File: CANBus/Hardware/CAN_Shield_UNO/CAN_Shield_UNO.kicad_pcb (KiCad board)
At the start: 2 copper layers, 68.6 x 53.3 mm, 15 parts, among them J1 Power, J2 Digital/PWM, J3 Analog, J4 Digital/PWM, J7 Screw_Terminal_01x02, U2 TCAN1051HGV

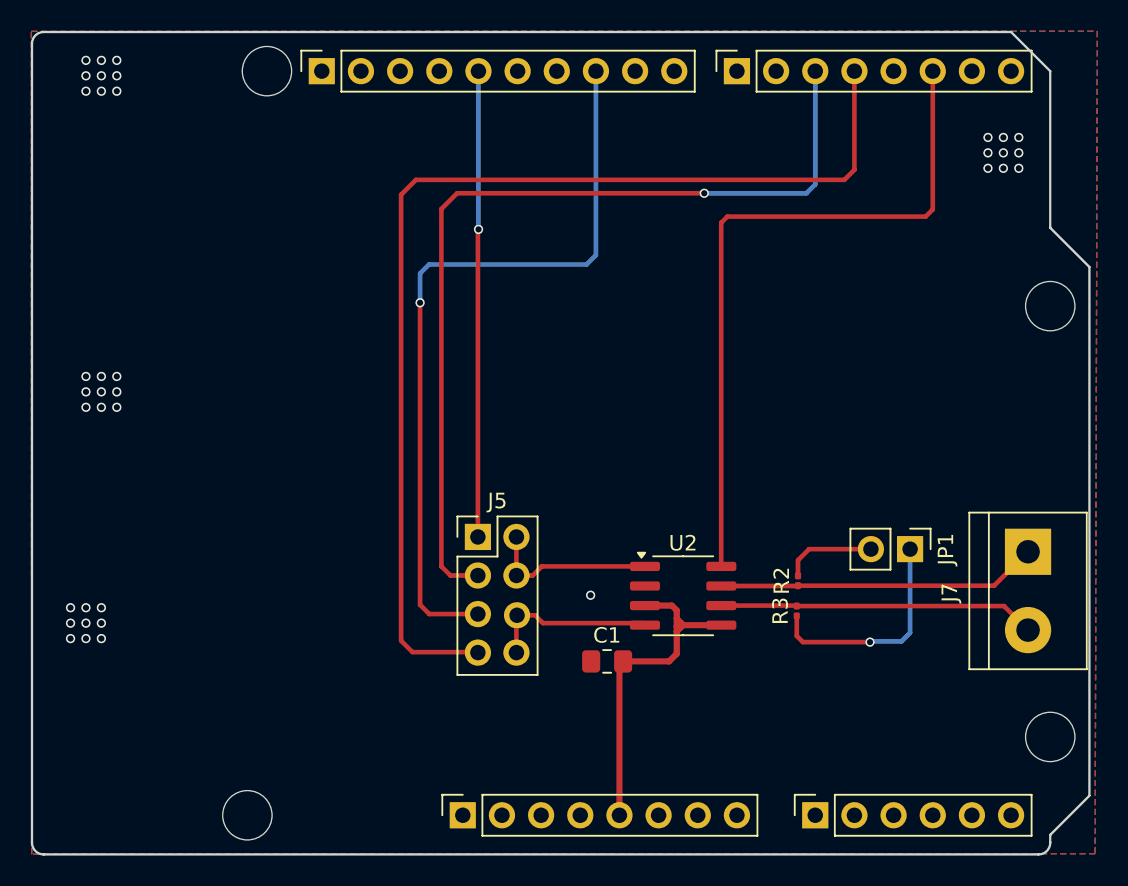
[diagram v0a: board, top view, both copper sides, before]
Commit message: feat: Resistors got changed
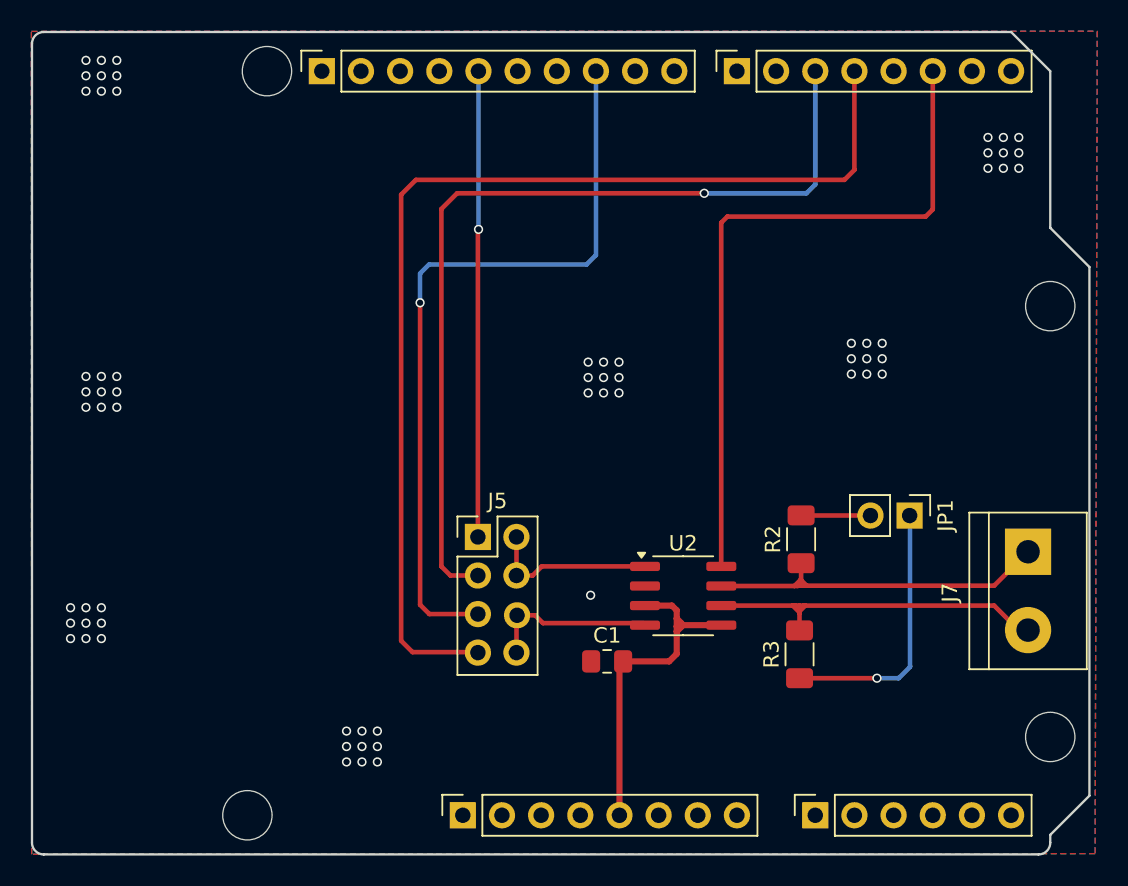
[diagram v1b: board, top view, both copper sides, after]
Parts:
- R2, R3: footprint Resistor_SMD:R_0201_0603Metric -> Resistor_SMD:R_1206_3216Metric_Pad1.30x1.75mm_HandSolder
- moved R3 2.82 mm to (149.8, 87.0)
- moved R2 2.70 mm to (149.9, 79.6)
- moved JP1 2.18 mm to (156.9, 78.0)
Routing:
- net Net-(J7-Pin_2): track 20.6 -> 24.4 mm
- net Net-(JP1-A): track 14.5 -> 17.3 mm
- net Net-(J7-Pin_1): track 20.8 -> 23.4 mm
- net Net-(JP1-B): track 6.04 -> 4.50 mm
- net GND: vias 37 -> 64

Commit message: feat(Hw): Route PCB
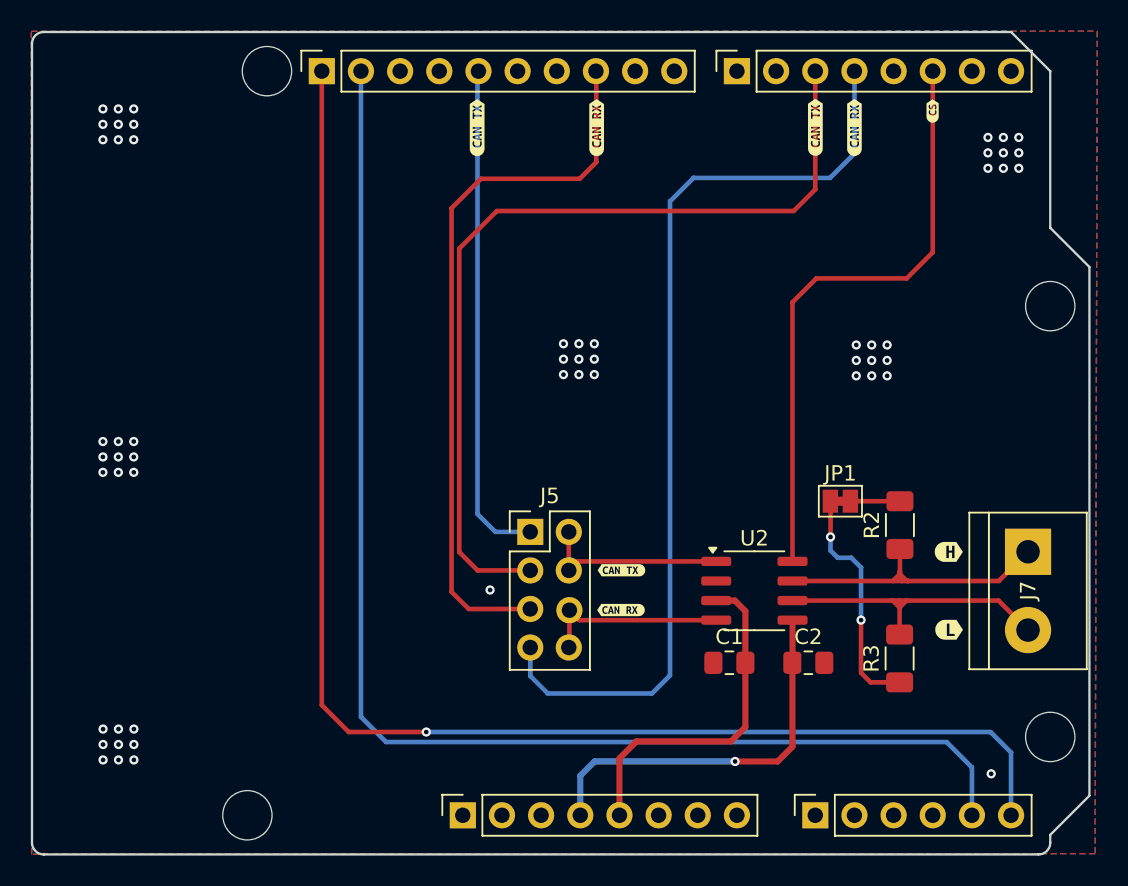
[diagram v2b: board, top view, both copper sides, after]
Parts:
- added C2: 0.1u, Capacitor_SMD:C_0805_2012Metric_Pad1.18x1.45mm_HandSolder, F.Cu at (150.3, 87.6)
- added kibuzzard-6616FE73: G***, kibuzzard-6616FE73, F.Cu at (138.2, 81.6)
- added kibuzzard-6616FEA4: G***, kibuzzard-6616FEA4, F.Cu at (138.2, 84.2)
- added kibuzzard-66170297: G***, kibuzzard-66170297, F.Cu at (150.8, 52.8)
- added kibuzzard-66170297: G***, kibuzzard-66170297, F.Cu at (128.9, 52.9)
- added kibuzzard-661702AA: G***, kibuzzard-661702AA, F.Cu at (136.6, 52.9)
- added kibuzzard-661702AA: G***, kibuzzard-661702AA, F.Cu at (153.3, 52.9)
- added kibuzzard-6617034B: G***, kibuzzard-6617034B, F.Cu at (159.5, 80.4)
- added kibuzzard-6617035A: G***, kibuzzard-6617035A, F.Cu at (159.5, 85.4)
- added kibuzzard-661705A6: G***, kibuzzard-661705A6, F.Cu at (158.4, 51.8)
- JP1: footprint Connector_PinHeader_2.54mm:PinHeader_1x02_P2.54mm_Vertical -> Jumper:SolderJumper-2_P1.3mm_Bridged_Pad1.0x1.5mm
- moved C1 7.93 mm to (145.2, 87.6)
- moved R3 6.50 mm to (156.3, 87.3)
- moved R2 6.48 mm to (156.3, 78.6)
- moved U2 4.63 mm to (146.8, 82.9)
- moved JP1 4.59 mm to (152.4, 77.1), turned to 0 degrees
- moved J5 3.41 mm to (132.3, 79.1)
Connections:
- U2 pad 5: +5V -> +3V3
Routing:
- net /SCL/A5: track 0.00 -> 91.2 mm, vias 0 -> 1
- net /SDA/A4: track 0.00 -> 86.0 mm
- net +3V3: track 0.00 -> 25.3 mm, vias 0 -> 1
- net /CTX0_MINIMA: track 70.7 -> 61.2 mm
- net /2: track 45.3 -> 39.0 mm
- net Net-(J7-Pin_2): track 24.4 -> 19.6 mm
- net Net-(J7-Pin_1): track 23.4 -> 19.7 mm
- net /CRX0_WIFI: track 30.2 -> 32.7 mm, vias 1 -> 0
- net /CTX0_WIFI: track 49.3 -> 47.0 mm, vias 1 -> 0
- net Net-(JP1-A): track 17.3 -> 15.2 mm, vias 1 -> 2
- net Net-(JP1-B): track 4.50 -> 3.21 mm
- net Net-(J5-Pin_5): track 11.0 -> 12.2 mm
- net Net-(J5-Pin_7): track 11.1 -> 12.3 mm
- net /CRX0_MINIMA: track 58.1 -> 57.1 mm, vias 1 -> 0
- net GND: vias 64 -> 56

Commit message: feat(hw): add logos and labels for UNO
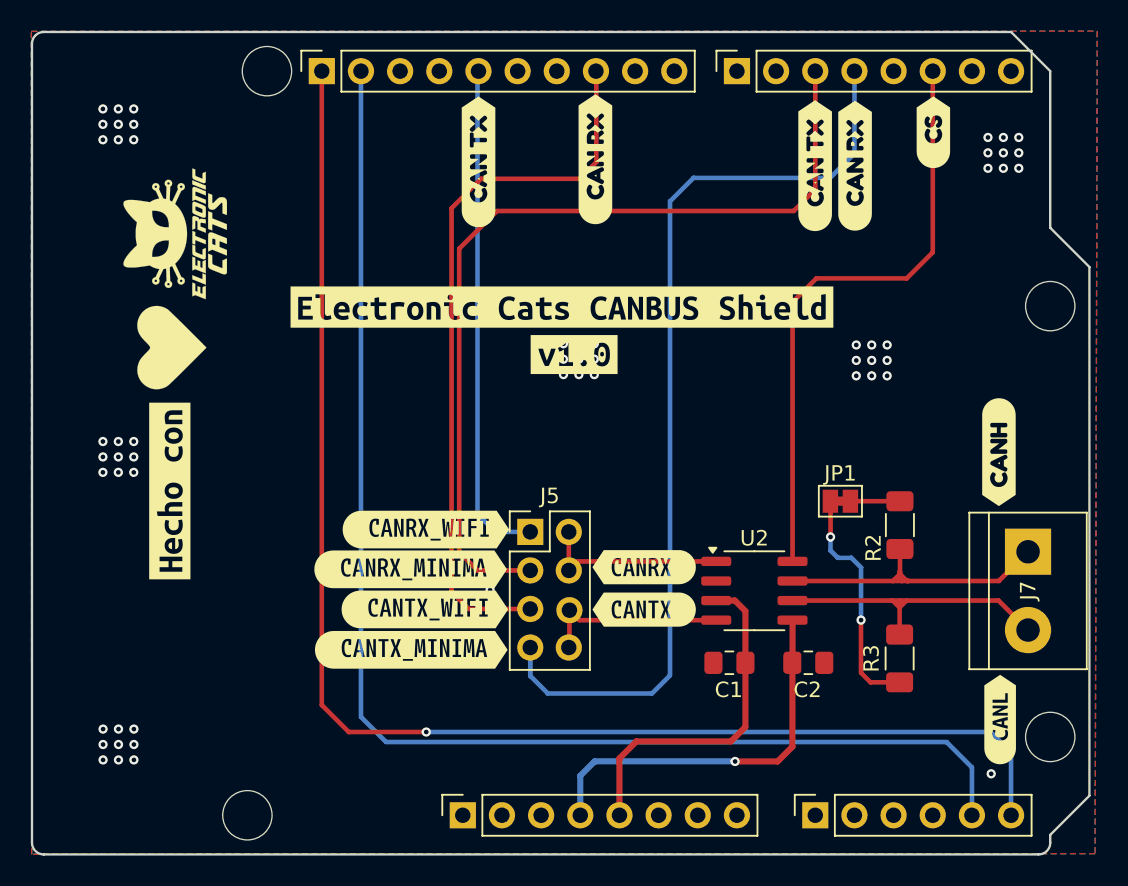
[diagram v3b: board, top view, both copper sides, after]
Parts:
- removed kibuzzard-6616FE73: G***, kibuzzard-6616FE73
- removed kibuzzard-6616FEA4: G***, kibuzzard-6616FEA4
- removed kibuzzard-66170297 (x2): G***, kibuzzard-66170297
- removed kibuzzard-661702AA (x2): G***, kibuzzard-661702AA
- removed kibuzzard-6617034B: G***, kibuzzard-6617034B
- removed kibuzzard-6617035A: G***, kibuzzard-6617035A
- removed kibuzzard-661705A6: G***, kibuzzard-661705A6
- added G***: LOGO, Aesthetics:electronic_cats_logo_8x6, F.Cu at (109.3, 59.8)
- added G***: LOGO, Aesthetics:electronic_cats_logo_8x6, B.Cu at (109.1, 78.8)
- added Ref**: Val**, Aesthetics:heart, F.Cu at (109.0, 71.4)
- added Ref**: Val**, Aesthetics:heart, B.Cu at (109.1, 67.1)
- added kibuzzard-661820F9: G***, kibuzzard-661820F9, F.Cu at (108.9, 76.4)
- added kibuzzard-661820F9: G***, kibuzzard-661820F9, B.Cu at (108.8, 62.1)
- added kibuzzard-66182154: G***, kibuzzard-66182154, F.Cu at (134.4, 64.5)
- added kibuzzard-66182154: G***, kibuzzard-66182154, B.Cu at (135.9, 64.5)
- added kibuzzard-6618216B: G***, kibuzzard-6618216B, F.Cu at (135.2, 67.6)
- added kibuzzard-6618216B: G***, kibuzzard-6618216B, B.Cu at (135.1, 67.6)
- added kibuzzard-66182400: G***, kibuzzard-66182400, F.Cu at (129.0, 55.1)
- added kibuzzard-66182409: G***, kibuzzard-66182409, F.Cu at (136.5, 54.9)
- added kibuzzard-66182412: G***, kibuzzard-66182412, F.Cu at (150.8, 55.3)
- added kibuzzard-66182419: G***, kibuzzard-66182419, F.Cu at (153.4, 55.3)
- added kibuzzard-66182422: G***, kibuzzard-66182422, F.Cu at (158.5, 53.2)
- added kibuzzard-66182455: G***, kibuzzard-66182455, F.Cu at (162.8, 91.2)
- added kibuzzard-6618247C: G***, kibuzzard-6618247C, F.Cu at (162.7, 73.9)
- added kibuzzard-661826AE: G***, kibuzzard-661826AE, F.Cu at (139.7, 81.4)
- added kibuzzard-661826C2: G***, kibuzzard-661826C2, F.Cu at (139.7, 84.1)
- added kibuzzard-66182706: G***, kibuzzard-66182706, F.Cu at (125.5, 78.9)
- added kibuzzard-6618271B: G***, kibuzzard-6618271B, F.Cu at (125.5, 84.1)
- added kibuzzard-6618272A: G***, kibuzzard-6618272A, F.Cu at (124.6, 86.7)
- added kibuzzard-66182736: G***, kibuzzard-66182736, F.Cu at (124.6, 81.5)

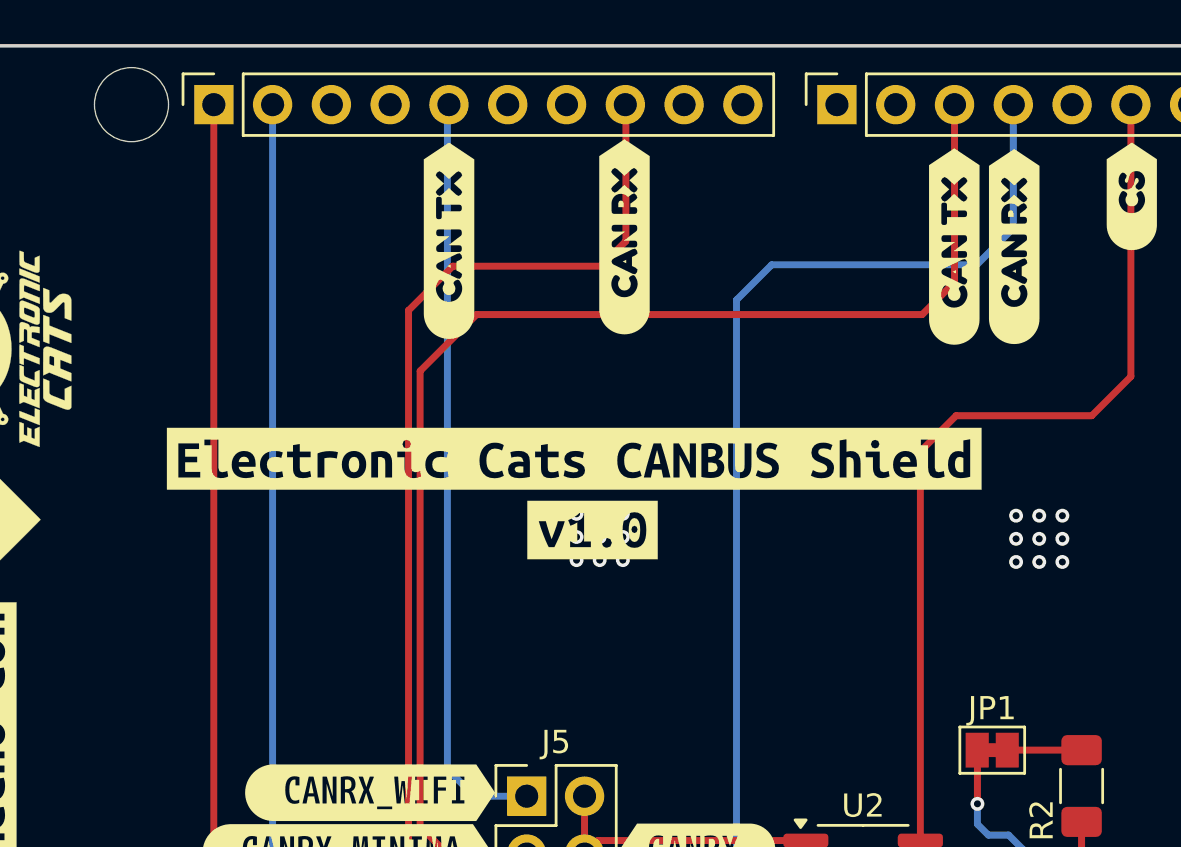
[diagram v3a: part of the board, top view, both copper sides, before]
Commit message: feat(hw): add labels pins
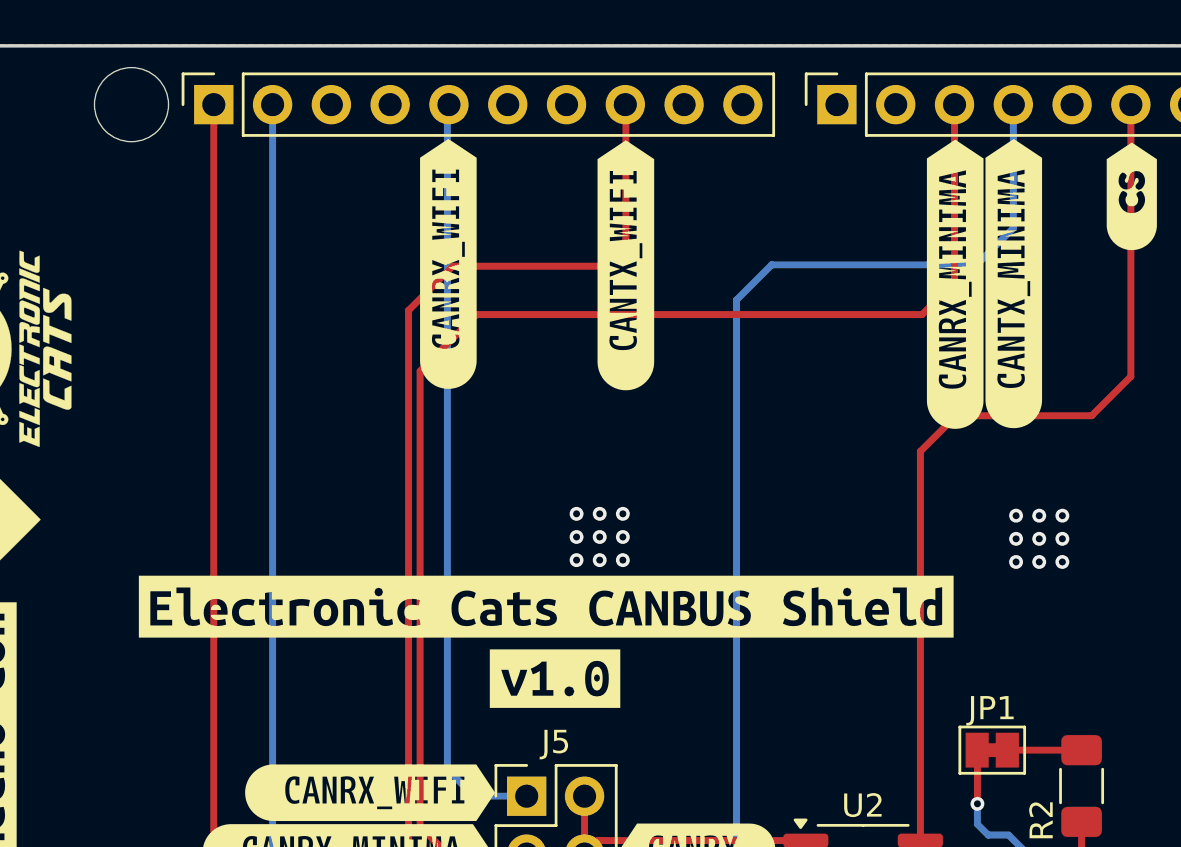
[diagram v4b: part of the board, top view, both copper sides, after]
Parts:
- removed kibuzzard-66182400: G***, kibuzzard-66182400
- removed kibuzzard-66182409: G***, kibuzzard-66182409
- removed kibuzzard-66182412: G***, kibuzzard-66182412
- removed kibuzzard-66182419: G***, kibuzzard-66182419
- added kibuzzard-66182965: G***, kibuzzard-66182965, F.Cu at (136.6, 56.1)
- added kibuzzard-66182980: G***, kibuzzard-66182980, F.Cu at (128.9, 56.1)
- added kibuzzard-661829B1: G***, kibuzzard-661829B1, F.Cu at (150.8, 57.0)
- added kibuzzard-661829C4: G***, kibuzzard-661829C4, F.Cu at (153.4, 56.9)
- moved kibuzzard-6618216B 6.90 mm to (134.0, 74.4)
- moved kibuzzard-6618216B 6.62 mm to (133.5, 74.0)
- moved kibuzzard-66182154 6.50 mm to (133.2, 70.9)
- moved kibuzzard-66182154 6.50 mm to (134.7, 70.9)

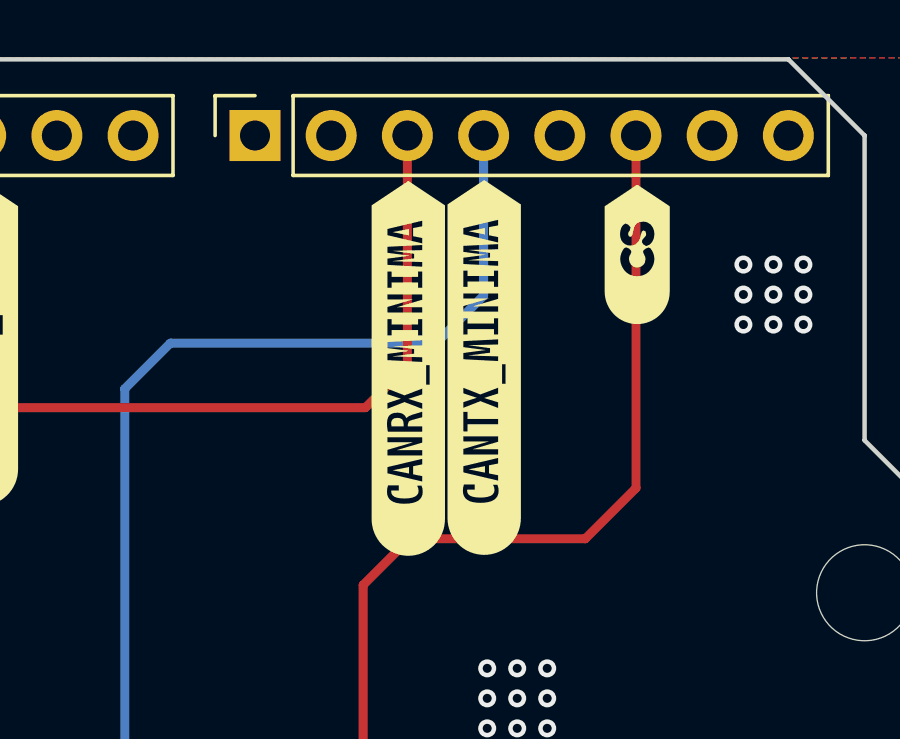
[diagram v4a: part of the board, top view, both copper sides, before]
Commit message: fix(hw): orientation labels UNO
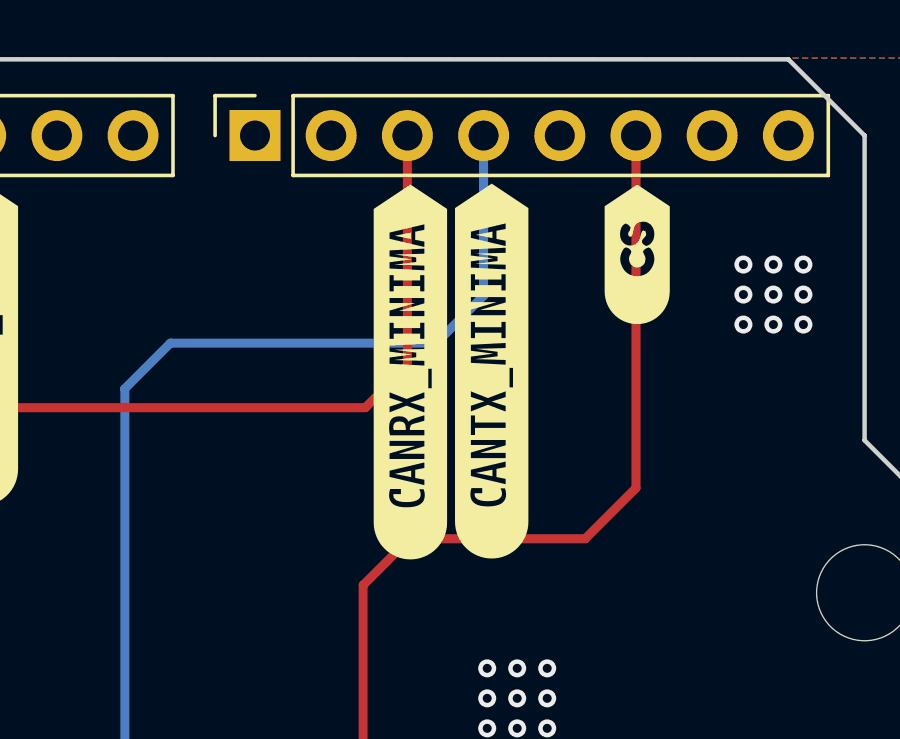
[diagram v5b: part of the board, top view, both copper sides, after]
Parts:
- moved kibuzzard-661829C4 0.28 mm to (153.6, 57.0)
- moved kibuzzard-661829B1 0.14 mm to (150.9, 57.1)
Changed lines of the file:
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@@
 	(footprint "kibuzzard-661829B1"
 		(layer "F.Cu")
-		(at 150.83 56.96 90)
+		(at 150.9 57.08 90)
 		(descr "Generated with KiBuzzard")
 		(tags "kb_params=eyJBbGlnbm1lbnRDaG9pY2UiOiAiQ2VudGVyIiwgIkNhcExlZnRDaG9pY2UiOiAiKCIsICJDYXBSaWdodENob2ljZSI6ICI+IiwgIkZvbnRDb21ib0JveCI6ICJtcGx1cy0xbW4tbWVkaXVtIiwgIkhlaWdodEN0cmwiOiAiMSIsICJMYXllckNvbWJvQm94IjogIkYuU2lsa1MiLCAiTXVsdGlMaW5lVGV4dCI6ICJDQU5SWF9NSU5JTUEiLCAiUGFkZGluZ0JvdHRvbUN0cmwiOiAiIiwgIlBhZGRpbmdMZWZ0Q3RybCI6ICIiLCAiUGFkZGluZ1JpZ2h0Q3RybCI6ICIiLCAiUGFkZGluZ1RvcEN0cmwiOiAiIiwgIldpZHRoQ3RybCI6ICIifQ==")
@@
 	(footprint "kibuzzard-661829C4"
 		(layer "F.Cu")
-		(at 153.36 56.93 90)
+		(at 153.61 57.05 90)
 		(descr "Generated with KiBuzzard")
 		(tags "kb_params=eyJBbGlnbm1lbnRDaG9pY2UiOiAiQ2VudGVyIiwgIkNhcExlZnRDaG9pY2UiOiAiKCIsICJDYXBSaWdodENob2ljZSI6ICI+IiwgIkZvbnRDb21ib0JveCI6ICJtcGx1cy0xbW4tbWVkaXVtIiwgIkhlaWdodEN0cmwiOiAiMSIsICJMYXllckNvbWJvQm94IjogIkYuU2lsa1MiLCAiTXVsdGlMaW5lVGV4dCI6ICJDQU5UWF9NSU5JTUEiLCAiUGFkZGluZ0JvdHRvbUN0cmwiOiAiIiwgIlBhZGRpbmdMZWZ0Q3RybCI6ICIiLCAiUGFkZGluZ1JpZ2h0Q3RybCI6ICIiLCAiUGFkZGluZ1RvcEN0cmwiOiAiIiwgIldpZHRoQ3RybCI6ICIifQ==")
